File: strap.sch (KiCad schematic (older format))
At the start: 20 parts, among them SW1 SW_DIP_x08, U3 74LVC1G06, U4 74LVC1G06, U5 PCA9306, U8 24AA0x

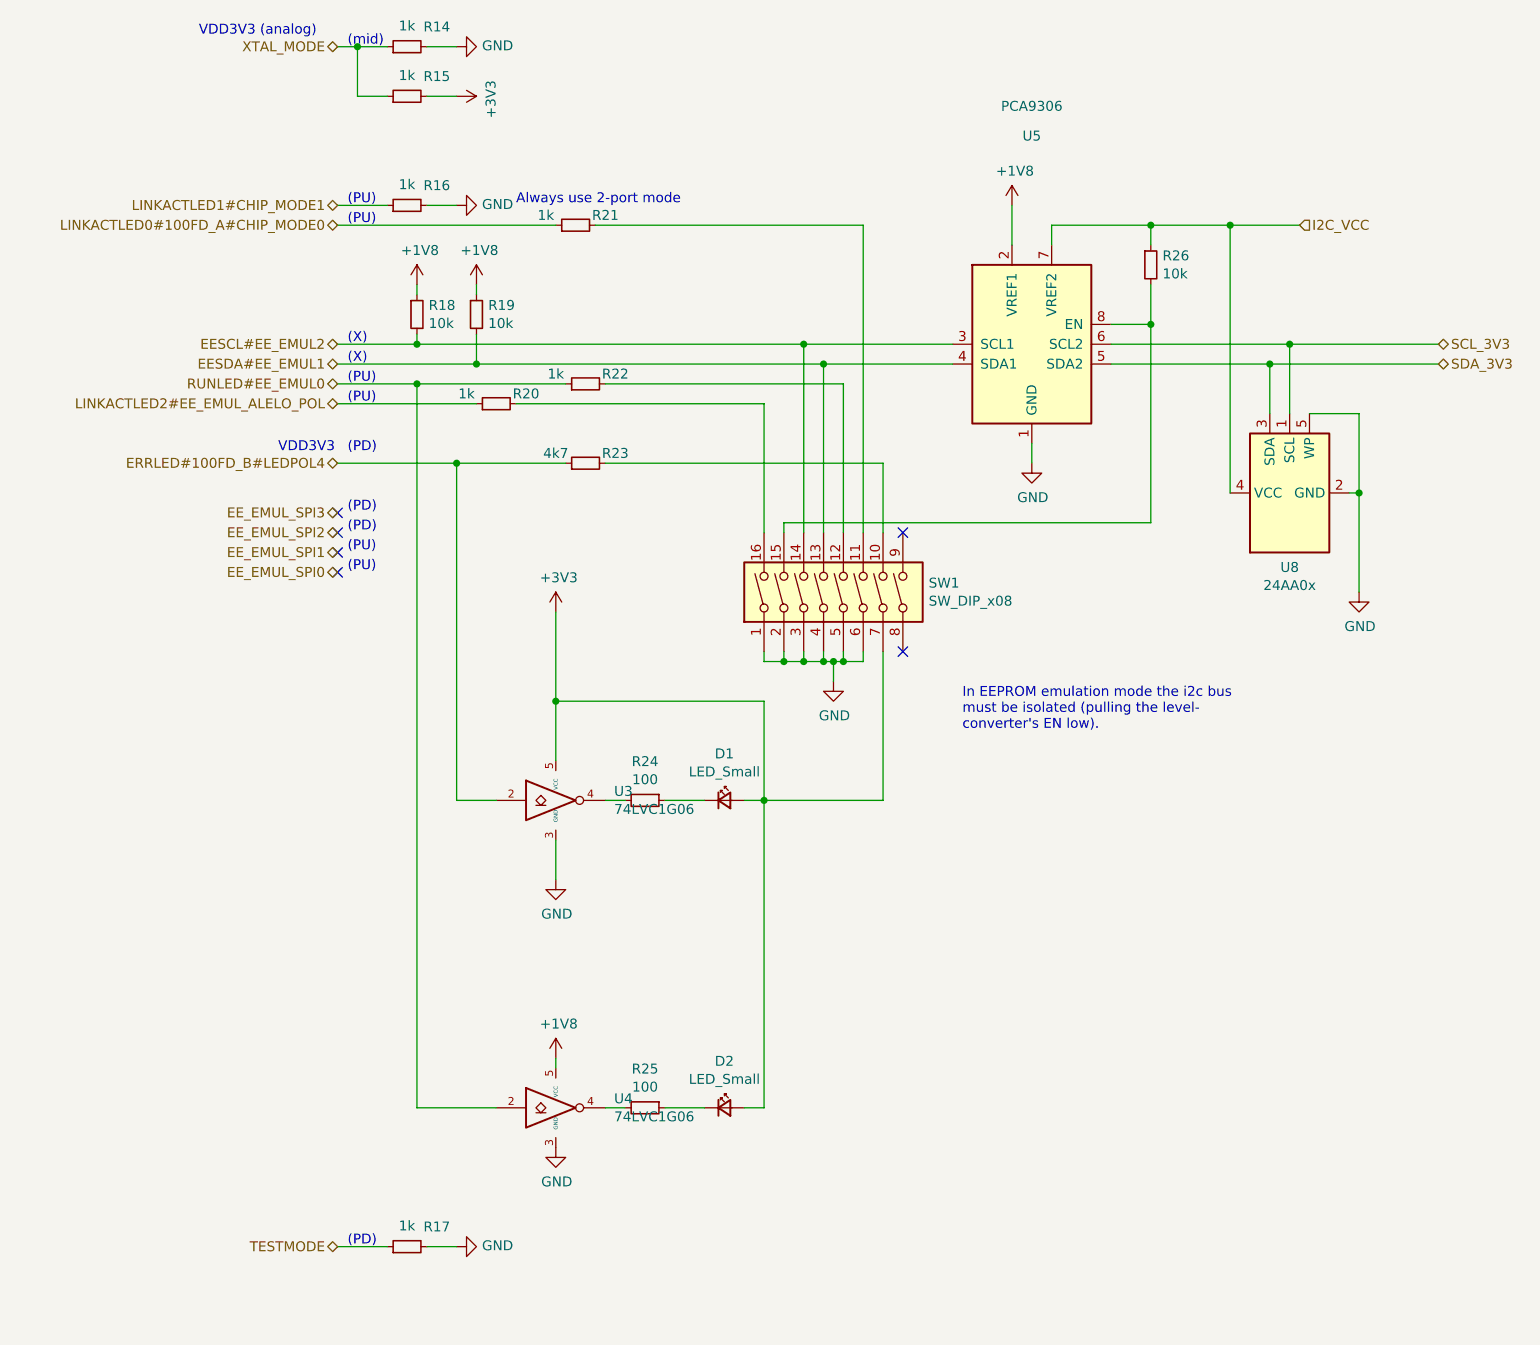
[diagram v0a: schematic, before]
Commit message: added I/O connectors, JTAG (just in case) and more
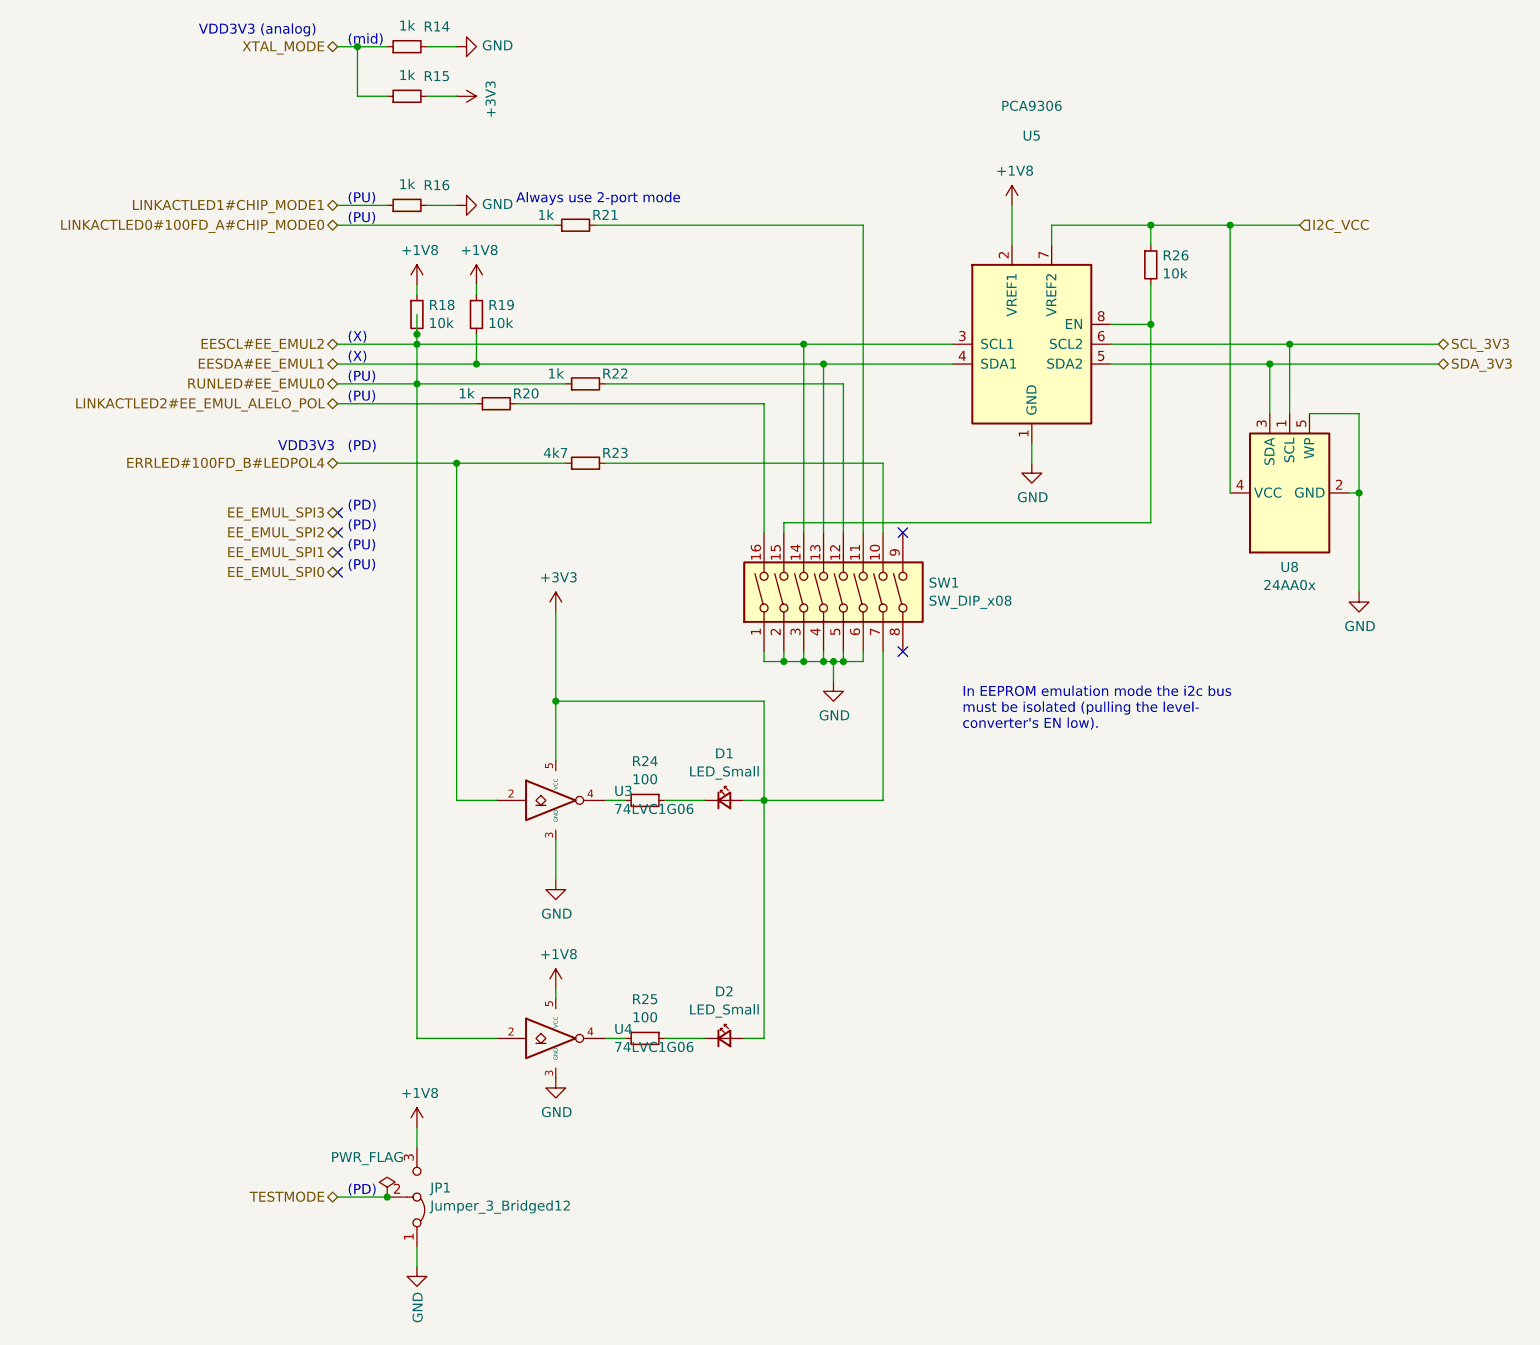
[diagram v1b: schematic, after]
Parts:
- removed R17: 1k, Resistor_SMD:R_0603_1608Metric, symbol Device:R_Small
- added JP1: Jumper_3_Bridged12, Connector_PinHeader_1.27mm:PinHeader_1x03_P1.27mm_Vertical, symbol Jumper:Jumper_3_Bridged12
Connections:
- net RUNLED#EE_EMUL0 is gone; now on net EESCL#EE_EMUL2: R22.1, U4.2
- net +1V8_lan9254: now also JP1.3 (B)
- net GND_lan9254: now also JP1.1 (A)
- net TESTMODE: now also JP1.2 (C)
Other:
- moved on the sheet: D2, R25, U4
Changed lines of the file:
@@
 $Descr A4 11693 8268
 encoding utf-8
-Sheet 4 4
+Sheet 4 6
 Title ""
 Date ""
@@
 L lan9254_project:GND #PWR?
 U 1 1 60EA51DE
-P 4900 6850
+P 4900 6500
 AR Path="/60DC28BD/60EA51DE" Ref="#PWR?"  Part="1"
 AR Path="/60E5E32B/60EA51DE" Ref="#PWR?"  Part="1"
 AR Path="/60DB2574/60E5E32B/60EA51DE" Ref="#PWR?"  Part="1"
-F 0 "#PWR?" H 4900 6600 50  0001 C CNN
-F 1 "GND" H 4905 6677 50  0000 C CNN
-F 2 "" H 4900 6850 50  0001 C CNN
-F 3 "" H 4900 6850 50  0001 C CNN
-	1    4900 6850
+F 0 "#PWR?" H 4900 6250 50  0001 C CNN
+F 1 "GND" H 4905 6327 50  0000 C CNN
+F 2 "" H 4900 6500 50  0001 C CNN
+F 3 "" H 4900 6500 50  0001 C CNN
+	1    4900 6500
 	1    0    0    -1
 $EndComp
@@
 L Device:R_Small R?
 U 1 1 60EA51EB
-P 5350 6650
+P 5350 6300
 AR Path="/60DC28BD/60EA51EB" Ref="R?"  Part="1"
 AR Path="/60E5E32B/60EA51EB" Ref="R25"  Part="1"
 AR Path="/60DB2574/60E5E32B/60EA51EB" Ref="R25"  Part="1"
-F 0 "R25" V 5154 6650 50  0000 C CNN
-F 1 "100" V 5245 6650 50  0000 C CNN
-F 2 "Resistor_SMD:R_0603_1608Metric" H 5350 6650 50  0001 C CNN
-F 3 "~" H 5350 6650 50  0001 C CNN
-	1    5350 6650
+F 0 "R25" V 5154 6300 50  0000 C CNN
+F 1 "100" V 5245 6300 50  0000 C CNN
+F 2 "Resistor_SMD:R_0603_1608Metric" H 5350 6300 50  0001 C CNN
+F 3 "~" H 5350 6300 50  0001 C CNN
+	1    5350 6300
 	0    1    1    0
 $EndComp
 Wire Wire Line
-	5150 6650 5250 6650
+	5150 6300 5250 6300
 $Comp
 L Device:LED_Small D2
 U 1 1 60EA51F6
-P 5750 6650
-F 0 "D2" H 5750 6885 50  0000 C CNN
-F 1 "LED_Small" H 5750 6794 50  0000 C CNN
-F 2 "LED_SMD:LED_0603_1608Metric" V 5750 6650 50  0001 C CNN
-F 3 "~" V 5750 6650 50  0001 C CNN
-	1    5750 6650
-	1    0    0    -1
-$EndComp
-Wire Wire Line
-	5650 6650 5450 6650
-Wire Wire Line
-	5950 6650 5850 6650
-Wire Wire Line
-	5950 5100 5950 6650
+P 5750 6300
+F 0 "D2" H 5750 6535 50  0000 C CNN
+F 1 "LED_Small" H 5750 6444 50  0000 C CNN
+F 2 "LED_SMD:LED_0603_1608Metric" V 5750 6300 50  0001 C CNN
+F 3 "~" V 5750 6300 50  0001 C CNN
+	1    5750 6300
+	1    0    0    -1
+$EndComp
+Wire Wire Line
+	5650 6300 5450 6300
+Wire Wire Line
+	5950 6300 5850 6300
 $Comp
 L lan9254_project:+1V8 #PWR?
 U 1 1 60EA9207
-P 4900 6400
+P 4900 6050
 AR Path="/60DC28BD/60EA9207" Ref="#PWR?"  Part="1"
 AR Path="/60E5E32B/60EA9207" Ref="#PWR?"  Part="1"
 AR Path="/60DB2574/60E5E32B/60EA9207" Ref="#PWR?"  Part="1"
-F 0 "#PWR?" H 4900 6250 50  0001 C CNN
-F 1 "+1V8" H 4915 6573 50  0000 C CNN
-F 2 "" H 4900 6400 50  0001 C CNN
-F 3 "" H 4900 6400 50  0001 C CNN
-	1    4900 6400
-	1    0    0    -1
-$EndComp
-Wire Wire Line
-	4200 3000 4200 6650
-Wire Wire Line
-	4200 6650 4600 6650
+F 0 "#PWR?" H 4900 5900 50  0001 C CNN
+F 1 "+1V8" H 4915 6223 50  0000 C CNN
+F 2 "" H 4900 6050 50  0001 C CNN
+F 3 "" H 4900 6050 50  0001 C CNN
+	1    4900 6050
+	1    0    0    -1
+$EndComp
+Wire Wire Line
+	4200 2650 4200 2750
+Wire Wire Line
+	4200 6300 4600 6300
 Connection ~ 4200 3000
 Wire Wire Line
@@
 	7900 2500 7900 2700
 Connection ~ 7900 2700
-Text HLabel 3800 7350 0    50   BiDi ~ 0
+Text HLabel 3800 7100 0    50   BiDi ~ 0
 TESTMODE
-Text Notes 3850 7350 0    50   ~ 0
+Text Notes 3850 7100 0    50   ~ 0
 (PD)
 $Comp
 L lan9254_project:GND #PWR?
 U 1 1 60EC3C97
-P 4400 7350
+P 4200 7450
 AR Path="/60DC28BD/60EC3C97" Ref="#PWR?"  Part="1"
 AR Path="/60E5E32B/60EC3C97" Ref="#PWR?"  Part="1"
 AR Path="/60DB2574/60E5E32B/60EC3C97" Ref="#PWR?"  Part="1"
-F 0 "#PWR?" H 4400 7100 50  0001 C CNN
-F 1 "GND" V 4405 7222 50  0000 R CNN
-F 2 "" H 4400 7350 50  0001 C CNN
-F 3 "" H 4400 7350 50  0001 C CNN
-	1    4400 7350
-	0    -1   -1   0
-$EndComp
-Wire Wire Line
-	4250 7350 4400 7350
+F 0 "#PWR?" H 4200 7200 50  0001 C CNN
+F 1 "GND" V 4205 7322 50  0000 R CNN
+F 2 "" H 4200 7450 50  0001 C CNN
+F 3 "" H 4200 7450 50  0001 C CNN
+	1    4200 7450
+	1    0    0    -1
+$EndComp
 $Comp
 L Device:R_Small R?
@@
 	3900 1300 3800 1300
 Wire Wire Line
-	3800 7350 4050 7350
+	3800 7100 4050 7100
 Text HLabel 8650 2200 2    50   Input ~ 0
 I2C_VCC
@@
 L fmc:74LVC1G06 U4
 U 1 1 611387E0
-P 4900 6650
-F 0 "U4" H 5194 6696 50  0000 L CNN
-F 1 "74LVC1G06" H 5194 6605 50  0000 L CNN
-F 2 "Package_TO_SOT_SMD:SOT-553" H 4900 6650 50  0001 C CNN
-F 3 "http://www.ti.com/lit/sg/scyt129e/scyt129e.pdf" H 4900 6650 50  0001 C CNN
-	1    4900 6650
-	1    0    0    -1
-$EndComp
-Wire Wire Line
-	4900 6400 4900 6450
+P 4900 6300
+F 0 "U4" H 5194 6346 50  0000 L CNN
+F 1 "74LVC1G06" H 5194 6255 50  0000 L CNN
+F 2 "Package_TO_SOT_SMD:SOT-553" H 4900 6300 50  0001 C CNN
+F 3 "http://www.ti.com/lit/sg/scyt129e/scyt129e.pdf" H 4900 6300 50  0001 C CNN
+	1    4900 6300
+	1    0    0    -1
+$EndComp
+Wire Wire Line
+	4900 6050 4900 6100
 $Comp
 L fmc:24AA0x U8
@@
 Connection ~ 8500 2900
 $Comp
-L Device:R_Small R?
-U 1 1 60EC3C8D
-P 4150 7350
-AR Path="/60DC28BD/60EC3C8D" Ref="R?"  Part="1"
-AR Path="/60E5E32B/60EC3C8D" Ref="R17"  Part="1"
-AR Path="/60DB2574/60E5E32B/60EC3C8D" Ref="R17"  Part="1"
-F 0 "R17" V 4250 7200 50  0000 C CNN
-F 1 "1k" V 4255 7350 50  0000 C CNN
-F 2 "Resistor_SMD:R_0603_1608Metric" H 4150 7350 50  0001 C CNN
-F 3 "~" H 4150 7350 50  0001 C CNN
-	1    4150 7350
-	0    -1   -1   0
-$EndComp
-$Comp
 L Switch:SW_DIP_x08 SW1
 U 1 1 60E7D790
@@
 $EndComp
 Wire Wire Line
-	5950 5100 5950 4600
-Wire Wire Line
 	5950 4600 4900 4600
 Connection ~ 5950 5100
@@
 NoConn ~ 6650 4350
 NoConn ~ 6650 3750
+$Comp
+L Jumper:Jumper_3_Bridged12 JP1
+U 1 1 60E8D294
+P 4200 7100
+F 0 "JP1" V 4246 7167 50  0000 L CNN
+F 1 "Jumper_3_Bridged12" V 4155 7167 50  0000 L CNN
+F 2 "Connector_PinHeader_1.27mm:PinHeader_1x03_P1.27mm_Vertical" H 4200 7100 50  0001 C CNN
+F 3 "~" H 4200 7100 50  0001 C CNN
+	1    4200 7100
+	0    1    -1   0
+$EndComp
+Connection ~ 4200 2750
+Wire Wire Line
+	4200 2800 4200 3000
+Wire Wire Line
+	4200 3000 4200 6300
+Wire Wire Line
+	5950 5100 5950 6300
+Wire Wire Line
+	5950 4600 5950 5100
+Wire Wire Line
+	4200 7350 4200 7450
+$Comp
+L lan9254_project:+1V8 #PWR?
+U 1 1 60E9647B
+P 4200 6750
+AR Path="/60DC28BD/60E9647B" Ref="#PWR?"  Part="1"
+AR Path="/60E5E32B/60E9647B" Ref="#PWR?"  Part="1"
+AR Path="/60DB2574/60E5E32B/60E9647B" Ref="#PWR?"  Part="1"
+F 0 "#PWR?" H 4200 6600 50  0001 C CNN
+F 1 "+1V8" H 4215 6923 50  0000 C CNN
+F 2 "" H 4200 6750 50  0001 C CNN
+F 3 "" H 4200 6750 50  0001 C CNN
+	1    4200 6750
+	1    0    0    -1
+$EndComp
+Wire Wire Line
+	4200 6750 4200 6850
+$Comp
+L power:PWR_FLAG #FLG?
+U 1 1 60ECDB6A
+P 4050 7100
+F 0 "#FLG?" H 4050 7175 50  0001 C CNN
+F 1 "PWR_FLAG" H 3950 7300 50  0000 C CNN
+F 2 "" H 4050 7100 50  0001 C CNN
+F 3 "~" H 4050 7100 50  0001 C CNN
+	1    4050 7100
+	1    0    0    -1
+$EndComp
+Connection ~ 4050 7100
 $EndSCHEMATC
